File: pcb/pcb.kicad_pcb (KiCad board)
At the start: 2 copper layers, 19 parts, among them J1 RLD IN, J2 SPI Config, J3 RST, J4 Conn_01x02_Pin, J5 Power Supply, U1 ADS1293CISQ/NOPB

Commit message: Circuit Board Improvements
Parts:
- added D1: LED_Filled, LED_SMD:LED_0201_0603Metric_Pad0.64x0.40mm_HandSolder, F.Cu at (119.4, 61.0)
- added R10: R_Small, Resistor_SMD:R_0402_1005Metric, F.Cu at (135.1, 71.7)
- added R11: R_Small, Resistor_SMD:R_0402_1005Metric, F.Cu at (135.1, 73.7)
- added R12: R_Small, Resistor_SMD:R_0201_0603Metric_Pad0.64x0.40mm_HandSolder, F.Cu at (119.6, 59.2)
- added R5: 1M Ohms, Resistor_SMD:R_0201_0603Metric_Pad0.64x0.40mm_HandSolder, F.Cu at (119.4, 76.6)
- added R6: 10kOHMs, Resistor_SMD:R_0201_0603Metric_Pad0.64x0.40mm_HandSolder, F.Cu at (132.1, 63.5)
- added R7: R_Small, Resistor_SMD:R_0402_1005Metric, F.Cu at (135.1, 65.7)
- added R8: R_Small, Resistor_SMD:R_0402_1005Metric, F.Cu at (135.1, 67.7)
- added R9: R_Small, Resistor_SMD:R_0402_1005Metric, F.Cu at (135.1, 69.7)
- C1, C3: value ~ -> 4.7nF
- C2: value ~ -> 4.7
- C4: value ~ -> 4.7 nF
- C6: value LESRC -> 1 uF
- J2: value SPI Config -> RLD OUT; footprint Connector_PinHeader_2.54mm:PinHeader_2x01_P2.54mm_Vertical -> Connector_PinHeader_2.54mm:PinHeader_1x01_P2.54mm_Vertical
- J4: value Conn_01x02_Pin -> Conn_01x06_Pin; footprint Connector_PinHeader_2.54mm:PinHeader_1x02_P2.54mm_Vertical -> Connector_PinHeader_2.54mm:PinHeader_1x06_P2.54mm_Vertical
- J5: value Power Supply -> Ext Power Supply
- R1, R2, R3, R4: value 100 OHMs -> 47k OHMs; footprint OptoDevice:R_LDR_4.9x4.2mm_P2.54mm_Vertical -> Resistor_SMD:R_0201_0603Metric_Pad0.64x0.40mm_HandSolder
- moved J5 41.4 mm to (119.4, 55.9)
- moved C5 37.0 mm to (126.1, 63.5)
- moved J3 34.5 mm to (135.6, 61.0)
- moved C6 25.1 mm to (128.2, 58.4), turned to 180 degrees
- moved J4 23.2 mm to (139.7, 73.7), turned to 180 degrees
- moved R4 22.7 mm to (129.5, 76.5), turned to 90 degrees
- moved U1 21.3 mm to (129.5, 68.6)
- moved R3 19.2 mm to (120.4, 71.1)
- moved IE1 17.7 mm to (114.3, 66.0)
- moved IE2 17.3 mm to (114.3, 71.1)
- moved IE3 17.0 mm to (114.3, 76.2)
- moved R2 16.0 mm to (120.4, 68.6)
- moved J1 14.8 mm to (116.8, 81.3), turned to 180 degrees
- moved J2 14.0 mm to (121.9, 76.2), turned to 90 degrees
- moved C1 13.5 mm to (123.7, 66.0)
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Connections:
- U1 pad 15: Net-(J2-Pin_1) -> Net-(J4-Pin_1)
- U1 pad 16: Net-(J2-Pin_2) -> Net-(U1-CSB)
- U1 pad 17: unconnected-(U1-SCLK-Pad17) -> Net-(U1-SCLK)
- U1 pad 18: Net-(J4-Pin_1) -> Net-(U1-SDI)
- U1 pad 19: Net-(J4-Pin_2) -> Net-(U1-SDO)
- U1 pad 20: unconnected-(U1-DRDYB-Pad20) -> Net-(U1-DRDYB)
- U1 pad 23: unconnected-(U1-XTAL1-Pad23) -> Net-(J5-Pin_2)
- U1 pad 24: unconnected-(U1-XTAL2-Pad24) -> Net-(U1-XTAL2)
- U1 pad 25: Net-(J3-Pin_1) -> unconnected-(U1-RSTB-Pad25)
- U1 pad 9: unconnected-(U1-RLDOUT-Pad9) -> Net-(U1-RLDOUT)
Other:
- board outline added: 33 x 30.5 mm

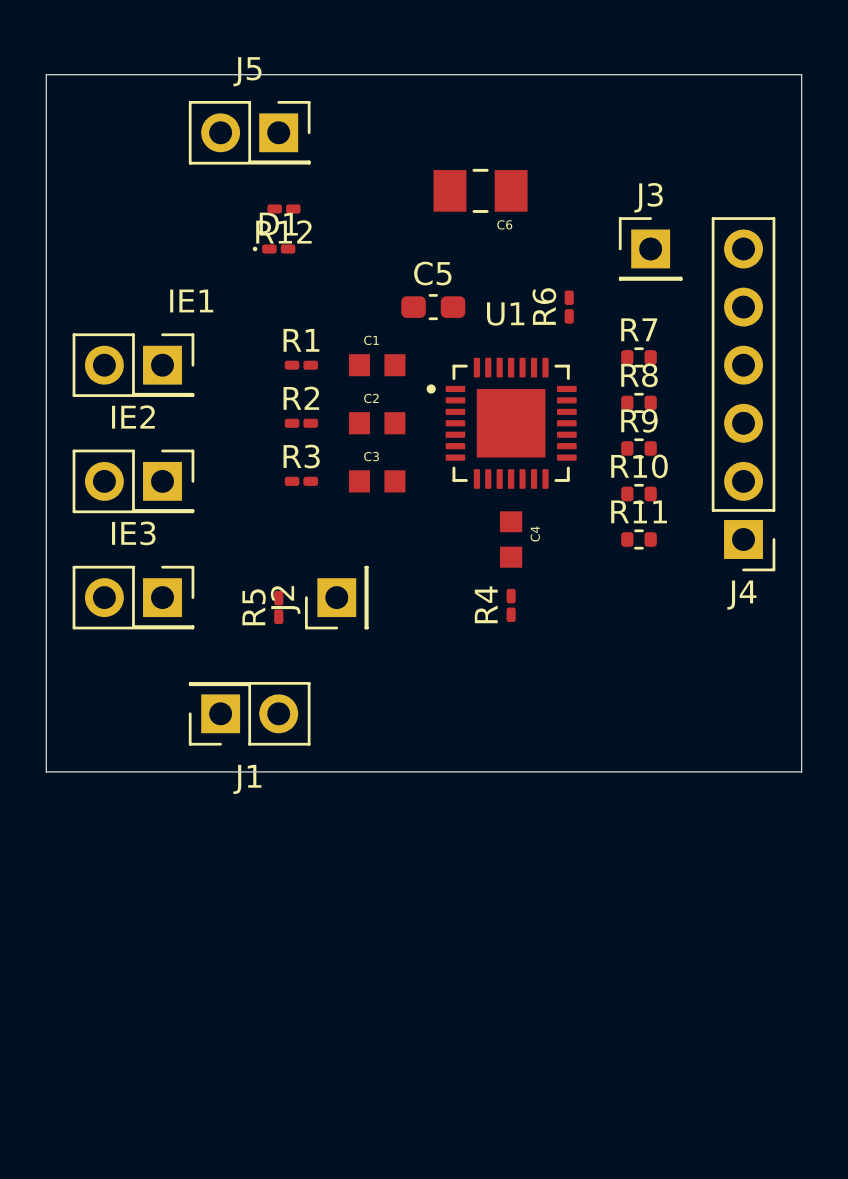
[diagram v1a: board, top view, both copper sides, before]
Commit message: track routing
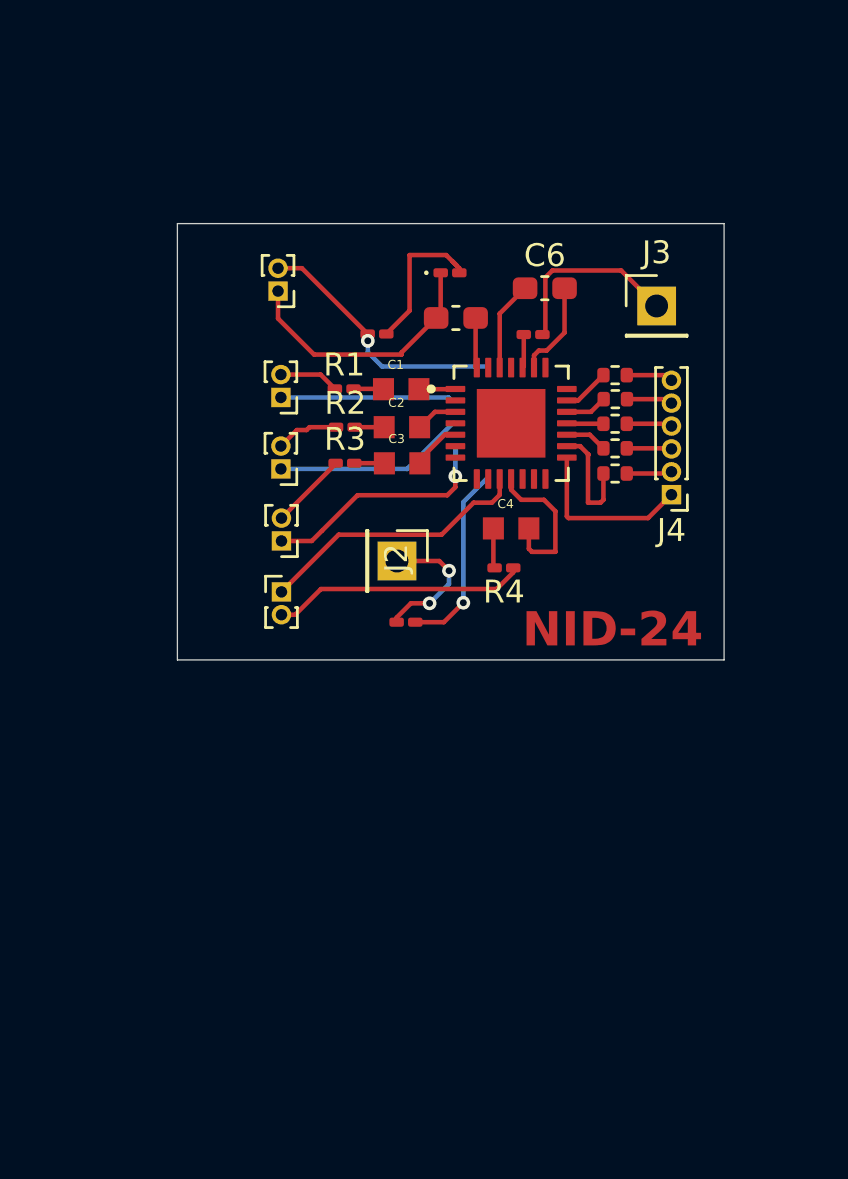
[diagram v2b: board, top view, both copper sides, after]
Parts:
- C6: footprint C3216X7S0J226M160AB:CAPC3216X180N -> Capacitor_SMD:C_0603_1608Metric_Pad1.08x0.95mm_HandSolder
- IE1, IE2, IE3, J1, J5: footprint Connector_PinSocket_2.54mm:PinSocket_2x01_P2.54mm_Vertical -> Connector_PinHeader_1.00mm:PinHeader_1x02_P1.00mm_Vertical
- J4: footprint Connector_PinHeader_2.54mm:PinHeader_1x06_P2.54mm_Vertical -> Connector_PinHeader_1.00mm:PinHeader_1x06_P1.00mm_Vertical
- moved D1 7.56 mm to (126.9, 62.0)
- moved J5 6.92 mm to (119.3, 62.8), turned to 180 degrees
- moved R12 6.81 mm to (123.7, 64.7)
- moved J1 5.96 mm to (119.5, 76.0), turned to 0 degrees
- moved IE3 5.76 mm to (119.5, 73.7), turned to 180 degrees
- moved R5 5.60 mm to (124.9, 77.3), turned to 0 degrees
- moved IE1 5.36 mm to (119.5, 67.5), turned to 180 degrees
- moved IE2 5.20 mm to (119.5, 70.6), turned to 180 degrees
- moved C6 5.10 mm to (131.0, 62.7), turned to 0 degrees
- moved J4 3.71 mm to (136.6, 71.7)
- moved J2 3.08 mm to (124.5, 74.6), turned to -90 degrees
- moved R11 3.07 mm to (134.1, 70.8)
- moved J3 2.50 mm to (135.9, 63.5)
- moved R10 2.25 mm to (134.1, 69.7)
- moved R1 2.14 mm to (122.2, 67.1)
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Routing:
- net Net-(J5-Pin_2): track 0.00 -> 15.8 mm, vias 0 -> 1
- net Net-(J1-Pin_1): track 0.00 -> 12.0 mm
- net Net-(D1-K): track 0.00 -> 11.5 mm
- net Net-(J1-Pin_2): track 0.00 -> 11.1 mm
- net Net-(IE3-Pin_1): track 0.00 -> 10.7 mm, vias 0 -> 1
- net Net-(IE2-Pin_1): track 0.00 -> 8.39 mm
- net Net-(U1-RLDOUT): track 0.00 -> 8.28 mm, vias 0 -> 1
- net Net-(J3-Pin_1): track 0.00 -> 8.18 mm
- net Net-(J4-Pin_1): track 0.00 -> 7.60 mm
- net Net-(IE1-Pin_1): track 0.00 -> 7.50 mm
- net Net-(D1-A): track 0.00 -> 6.75 mm
- net Net-(U1-RLDIN): track 0.00 -> 6.68 mm
- net Net-(J2-Pin_1): track 0.00 -> 6.13 mm, vias 0 -> 2
- net Net-(U1-CSB): track 0.00 -> 5.09 mm
- net Net-(U1-CVREF): track 0.00 -> 3.93 mm
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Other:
- board size 33 x 30.5 mm -> 23.9 x 19.1 mm
- board text added: "NID-24"

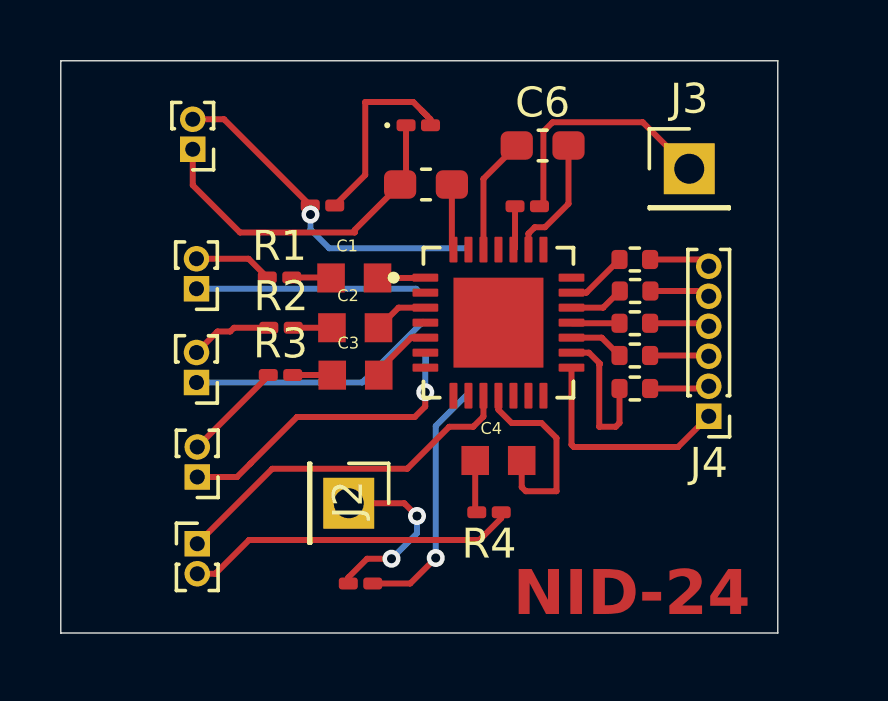
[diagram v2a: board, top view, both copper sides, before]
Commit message: reduced trace length from IE to Filters
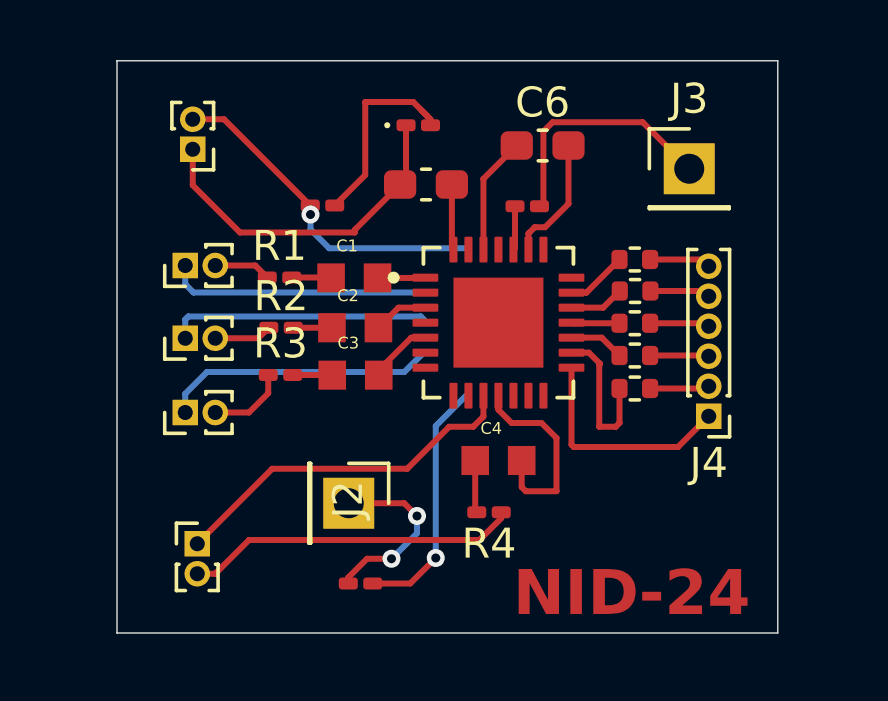
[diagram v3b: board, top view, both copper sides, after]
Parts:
- moved IE3 2.19 mm to (119.1, 71.6), turned to 90 degrees
- moved IE2 1.52 mm to (119.1, 69.1), turned to 90 degrees
- moved IE1 0.86 mm to (119.1, 66.7), turned to 90 degrees
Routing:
- net Net-(IE3-Pin_1): track 10.7 -> 9.11 mm, vias 1 -> 0
- net Net-(IE1-Pin_1): track 7.50 -> 8.79 mm
- net Net-(IE2-Pin_2): track 2.75 -> 1.93 mm
- net Net-(IE3-Pin_2): track 3.38 -> 2.64 mm
- net Net-(IE1-Pin_2): track 2.62 -> 1.90 mm
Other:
- board size 23.9 x 19.1 mm -> 22 x 19.1 mm
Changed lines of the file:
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@@
   )
   (footprint "Connector_PinHeader_1.00mm:PinHeader_1x02_P1.00mm_Vertical" (layer "F.Cu")
-    (at 119.5 73.725 180)
+    (at 119.1 71.575 90)
     (descr "Through hole straight pin header, 1x02, 1.00mm pitch, single row")
     (tags "Through hole pin header THT 1x02 1.00mm single row")
@@
     (property "ki_keywords" "connector")
     (attr through_hole)
-    (fp_text reference "IE3" (at 0 -1.56) (layer "F.SilkS") hide
-        (effects (font (size 1 1) (thickness 0.15)))
-    )
-    (fp_text value "Conn_02x01" (at 0 2.56) (layer "F.Fab") hide
-        (effects (font (size 1 1) (thickness 0.15)))
-    )
-    (fp_text user "${REFERENCE}" (at 0 0.5 90) (layer "F.Fab")
+    (fp_text reference "IE3" (at 0 -1.56 90) (layer "F.SilkS") hide
+        (effects (font (size 1 1) (thickness 0.15)))
+    )
+    (fp_text value "Conn_02x01" (at 0 2.56 90) (layer "F.Fab") hide
+        (effects (font (size 1 1) (thickness 0.15)))
+    )
+    (fp_text user "${REFERENCE}" (at 0 0.5) (layer "F.Fab")
         (effects (font (size 0.76 0.76) (thickness 0.114)))
     )
@@
     (fp_line (start 0.635 1.5) (end -0.635 1.5)
       (stroke (width 0.1) (type solid)) (layer "F.Fab"))
-    (pad "1" thru_hole rect (at 0 0 180) (size 0.85 0.85) (drill 0.5) (layers "*.Cu" "*.Mask")
+    (pad "1" thru_hole rect (at 0 0 90) (size 0.85 0.85) (drill 0.5) (layers "*.Cu" "*.Mask")
       (net 18 "Net-(IE3-Pin_1)") (pinfunction "Pin_1") (pintype "passive"))
-    (pad "2" thru_hole oval (at 0 1 180) (size 0.85 0.85) (drill 0.5) (layers "*.Cu" "*.Mask")
+    (pad "2" thru_hole oval (at 0 1 90) (size 0.85 0.85) (drill 0.5) (layers "*.Cu" "*.Mask")
       (net 19 "Net-(IE3-Pin_2)") (pinfunction "Pin_2") (pintype "passive"))
     (model "${KICAD6_3DMODEL_DIR}/Connector_PinHeader_1.00mm.3dshapes/PinHeader_1x02_P1.00mm_Vertical.wrl"
@@
   )
   (footprint "Connector_PinHeader_1.00mm:PinHeader_1x02_P1.00mm_Vertical" (layer "F.Cu")
-    (at 119.475 67.45 180)
+    (at 119.1 66.675 90)
     (descr "Through hole straight pin header, 1x02, 1.00mm pitch, single row")
     (tags "Through hole pin header THT 1x02 1.00mm single row")
@@
     (property "ki_keywords" "connector")
     (attr through_hole)
-    (fp_text reference "IE1" (at 0 -1.56) (layer "F.SilkS") hide
-        (effects (font (size 1 1) (thickness 0.15)))
-    )
-    (fp_text value "Conn_02x01" (at 0 2.56) (layer "F.Fab") hide
-        (effects (font (size 1 1) (thickness 0.15)))
-    )
-    (fp_text user "${REFERENCE}" (at 0 0.5 90) (layer "F.Fab")
+    (fp_text reference "IE1" (at 0 -1.56 90) (layer "F.SilkS") hide
+        (effects (font (size 1 1) (thickness 0.15)))
+    )
+    (fp_text value "Conn_02x01" (at 0 2.56 90) (layer "F.Fab") hide
+        (effects (font (size 1 1) (thickness 0.15)))
+    )
+    (fp_text user "${REFERENCE}" (at 0 0.5) (layer "F.Fab")
         (effects (font (size 0.76 0.76) (thickness 0.114)))
     )
@@
     (fp_line (start 0.635 1.5) (end -0.635 1.5)
       (stroke (width 0.1) (type solid)) (layer "F.Fab"))
-    (pad "1" thru_hole rect (at 0 0 180) (size 0.85 0.85) (drill 0.5) (layers "*.Cu" "*.Mask")
+    (pad "1" thru_hole rect (at 0 0 90) (size 0.85 0.85) (drill 0.5) (layers "*.Cu" "*.Mask")
       (net 14 "Net-(IE1-Pin_1)") (pinfunction "Pin_1") (pintype "passive"))
-    (pad "2" thru_hole oval (at 0 1 180) (size 0.85 0.85) (drill 0.5) (layers "*.Cu" "*.Mask")
+    (pad "2" thru_hole oval (at 0 1 90) (size 0.85 0.85) (drill 0.5) (layers "*.Cu" "*.Mask")
       (net 15 "Net-(IE1-Pin_2)") (pinfunction "Pin_2") (pintype "passive"))
     (model "${KICAD6_3DMODEL_DIR}/Connector_PinHeader_1.00mm.3dshapes/PinHeader_1x02_P1.00mm_Vertical.wrl"
@@
   )
   (footprint "Connector_PinHeader_1.00mm:PinHeader_1x02_P1.00mm_Vertical" (layer "F.Cu")
-    (at 119.475 70.575 180)
+    (at 119.1 69.1 90)
     (descr "Through hole straight pin header, 1x02, 1.00mm pitch, single row")
     (tags "Through hole pin header THT 1x02 1.00mm single row")
@@
     (property "ki_keywords" "connector")
     (attr through_hole)
-    (fp_text reference "IE2" (at 0 -1.56) (layer "F.SilkS") hide
-        (effects (font (size 1 1) (thickness 0.15)))
-    )
-    (fp_text value "Conn_02x01" (at 0 2.56) (layer "F.Fab") hide
-        (effects (font (size 1 1) (thickness 0.15)))
-    )
-    (fp_text user "${REFERENCE}" (at 0 0.5 90) (layer "F.Fab")
+    (fp_text reference "IE2" (at 0 -1.56 90) (layer "F.SilkS") hide
+        (effects (font (size 1 1) (thickness 0.15)))
+    )
+    (fp_text value "Conn_02x01" (at 0 2.56 90) (layer "F.Fab") hide
+        (effects (font (size 1 1) (thickness 0.15)))
+    )
+    (fp_text user "${REFERENCE}" (at 0 0.5) (layer "F.Fab")
         (effects (font (size 0.76 0.76) (thickness 0.114)))
     )
@@
     (fp_line (start 0.635 1.5) (end -0.635 1.5)
       (stroke (width 0.1) (type solid)) (layer "F.Fab"))
-    (pad "1" thru_hole rect (at 0 0 180) (size 0.85 0.85) (drill 0.5) (layers "*.Cu" "*.Mask")
+    (pad "1" thru_hole rect (at 0 0 90) (size 0.85 0.85) (drill 0.5) (layers "*.Cu" "*.Mask")
       (net 16 "Net-(IE2-Pin_1)") (pinfunction "Pin_1") (pintype "passive"))
-    (pad "2" thru_hole oval (at 0 1 180) (size 0.85 0.85) (drill 0.5) (layers "*.Cu" "*.Mask")
+    (pad "2" thru_hole oval (at 0 1 90) (size 0.85 0.85) (drill 0.5) (layers "*.Cu" "*.Mask")
       (net 17 "Net-(IE2-Pin_2)") (pinfunction "Pin_2") (pintype "passive"))
     (model "${KICAD6_3DMODEL_DIR}/Connector_PinHeader_1.00mm.3dshapes/PinHeader_1x02_P1.00mm_Vertical.wrl"
@@
     )
   )
-  (gr_rect (start 114.95 59.85) (end 138.85 78.925)
+  (gr_rect (start 116.825 59.85) (end 138.85 78.925)
     (stroke (width 0.05) (type default)) (fill none) (layer "Edge.Cuts"))
   (gr_text "NID-24" (at 130.025 78.475) (layer "F.Cu")
@@
   (segment (start 126.974999 61.5) (end 127.162499 61.687501) (width 0.2) (layer "F.Cu") (net 13))
   (segment (start 125.1 61.225) (end 126.699999 61.225) (width 0.2) (layer "F.Cu") (net 13))
-  (segment (start 126.8 67.45) (end 126.925 67.575) (width 0.2) (layer "B.Cu") (net 14))
-  (segment (start 119.475 67.45) (end 126.8 67.45) (width 0.2) (layer "B.Cu") (net 14))
-  (segment (start 121.21 66.45) (end 121.835 67.075) (width 0.2) (layer "F.Cu") (net 15))
-  (segment (start 119.475 66.45) (end 121.21 66.45) (width 0.2) (layer "F.Cu") (net 15))
-  (segment (start 119.475 70.575) (end 125 70.575) (width 0.2) (layer "B.Cu") (net 16))
-  (segment (start 125 70.575) (end 127.025 68.55) (width 0.2) (layer "B.Cu") (net 16))
-  (segment (start 120.175 68.875) (end 120.6 68.875) (width 0.2) (layer "F.Cu") (net 17))
-  (segment (start 120.725 68.75) (end 121.885 68.75) (width 0.2) (layer "F.Cu") (net 17))
-  (segment (start 120.6 68.875) (end 120.725 68.75) (width 0.2) (layer "F.Cu") (net 17))
-  (segment (start 119.475 69.575) (end 120.175 68.875) (width 0.2) (layer "F.Cu") (net 17))
-  (segment (start 122.825 71.725) (end 126.75 71.725) (width 0.2) (layer "F.Cu") (net 18))
-  (segment (start 126.75 71.725) (end 127.1 71.375) (width 0.2) (layer "F.Cu") (net 18))
-  (segment (start 119.5 73.725) (end 120.825 73.725) (width 0.2) (layer "F.Cu") (net 18))
-  (segment (start 127.1 71.375) (end 127.1 70.9) (width 0.2) (layer "F.Cu") (net 18))
-  (segment (start 121.275 73.275) (end 122.825 71.725) (width 0.2) (layer "F.Cu") (net 18))
-  (segment (start 120.825 73.725) (end 121.275 73.275) (width 0.2) (layer "F.Cu") (net 18))
-  (via (at 127.1 70.9) (size 0.6) (drill 0.3) (layers "F.Cu" "B.Cu") (net 18))
-  (segment (start 127.1 69.65) (end 127.125 69.625) (width 0.2) (layer "B.Cu") (net 18))
-  (segment (start 127.1 70.9) (end 127.1 69.65) (width 0.2) (layer "B.Cu") (net 18))
-  (segment (start 127.125 69.625) (end 127.125 69.95) (width 0.2) (layer "B.Cu") (net 18))
-  (segment (start 119.5 72.725) (end 121.8675 70.3575) (width 0.2) (layer "F.Cu") (net 19))
-  (segment (start 121.8675 70.3575) (end 121.8675 70.325) (width 0.2) (layer "F.Cu") (net 19))
+  (segment (start 119.375 67.575) (end 127.15 67.575) (width 0.2) (layer "B.Cu") (net 14))
+  (segment (start 119.1 66.675) (end 119.1 67.3) (width 0.2) (layer "B.Cu") (net 14))
+  (segment (start 119.1 67.3) (end 119.375 67.575) (width 0.2) (layer "B.Cu") (net 14))
+  (segment (start 120.1 66.675) (end 121.435 66.675) (width 0.2) (layer "F.Cu") (net 15))
+  (segment (start 121.435 66.675) (end 121.835 67.075) (width 0.2) (layer "F.Cu") (net 15))
+  (segment (start 119.1 68.475) (end 119.2 68.375) (width 0.2) (layer "B.Cu") (net 16))
+  (segment (start 119.1 69.1) (end 119.1 68.475) (width 0.2) (layer "B.Cu") (net 16))
+  (segment (start 119.2 68.375) (end 126.95 68.375) (width 0.2) (layer "B.Cu") (net 16))
+  (segment (start 126.95 68.375) (end 127.1 68.525) (width 0.2) (layer "B.Cu") (net 16))
+  (segment (start 120.1 69.1) (end 121.535 69.1) (width 0.2) (layer "F.Cu") (net 17))
+  (segment (start 121.535 69.1) (end 121.885 68.75) (width 0.2) (layer "F.Cu") (net 17))
+  (segment (start 119.1 71.575) (end 119.1 70.95) (width 0.2) (layer "B.Cu") (net 18))
+  (segment (start 119.1 70.95) (end 119.825 70.225) (width 0.2) (layer "B.Cu") (net 18))
+  (segment (start 119.825 70.225) (end 126.4 70.225) (width 0.2) (layer "B.Cu") (net 18))
+  (segment (start 126.4 70.225) (end 127.025 69.6) (width 0.2) (layer "B.Cu") (net 18))
+  (segment (start 121.225 71.575) (end 121.8675 70.9325) (width 0.2) (layer "F.Cu") (net 19))
+  (segment (start 120.1 71.575) (end 121.225 71.575) (width 0.2) (layer "F.Cu") (net 19))
+  (segment (start 121.8675 70.9325) (end 121.8675 70.325) (width 0.2) (layer "F.Cu") (net 19))
   (segment (start 128.7 72.05) (end 129.04 71.71) (width 0.2) (layer "F.Cu") (net 20))
   (segment (start 122 73.45) (end 126.5 73.45) (width 0.2) (layer "F.Cu") (net 20))
